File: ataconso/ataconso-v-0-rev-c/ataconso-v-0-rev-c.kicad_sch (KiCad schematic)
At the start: 22 parts, among them J1 Conn_02x05_Odd_Even, J2 AudioJack2_SwitchT, U1 TL072, U2 NE555D, U3 NE555D, U4 MC78L05_SO8

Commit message: agregar plantilla
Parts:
- removed U2, U3: NE555D, Package_DIP:DIP-8_W7.62mm_Socket_LongPads, symbol Timer:NE555D
- added U2: NA556, Package_SO:SOIC-14W_7.5x9mm_P1.27mm, symbol Timer:NA556
- C1, C2, C3, C4, C5, C6: footprint Capacitor_THT:C_Disc_D3.8mm_W2.6mm_P2.50mm -> (none)
- D1, D2: footprint Diode_THT:D_DO-41_SOD81_P10.16mm_Horizontal -> (none)
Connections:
- net +12V: now also U2.10 (~{RST}), U2.14 (VCC), U2.14 (VCC), U2.4 (~{RST})
- net GND: now also U2.7 (GND), U2.7 (GND)
- net at C5.1, R2.2: now also U2.12 (THRES), U2.13 (DISCH)
- net at C1.1, RV1.3: now also U2.2 (THRES), U2.6 (TRIG)
- net at C7.1: now also U2.9 (OUT)
- net at C6.1: now also U2.11 (CONT)
- net at R1.2, RV1.2: now also U2.1 (DISCH)
- net at C2.1: now also U2.3 (CONT)
- new net: U2.5 (OUT), U2.8 (TRIG)

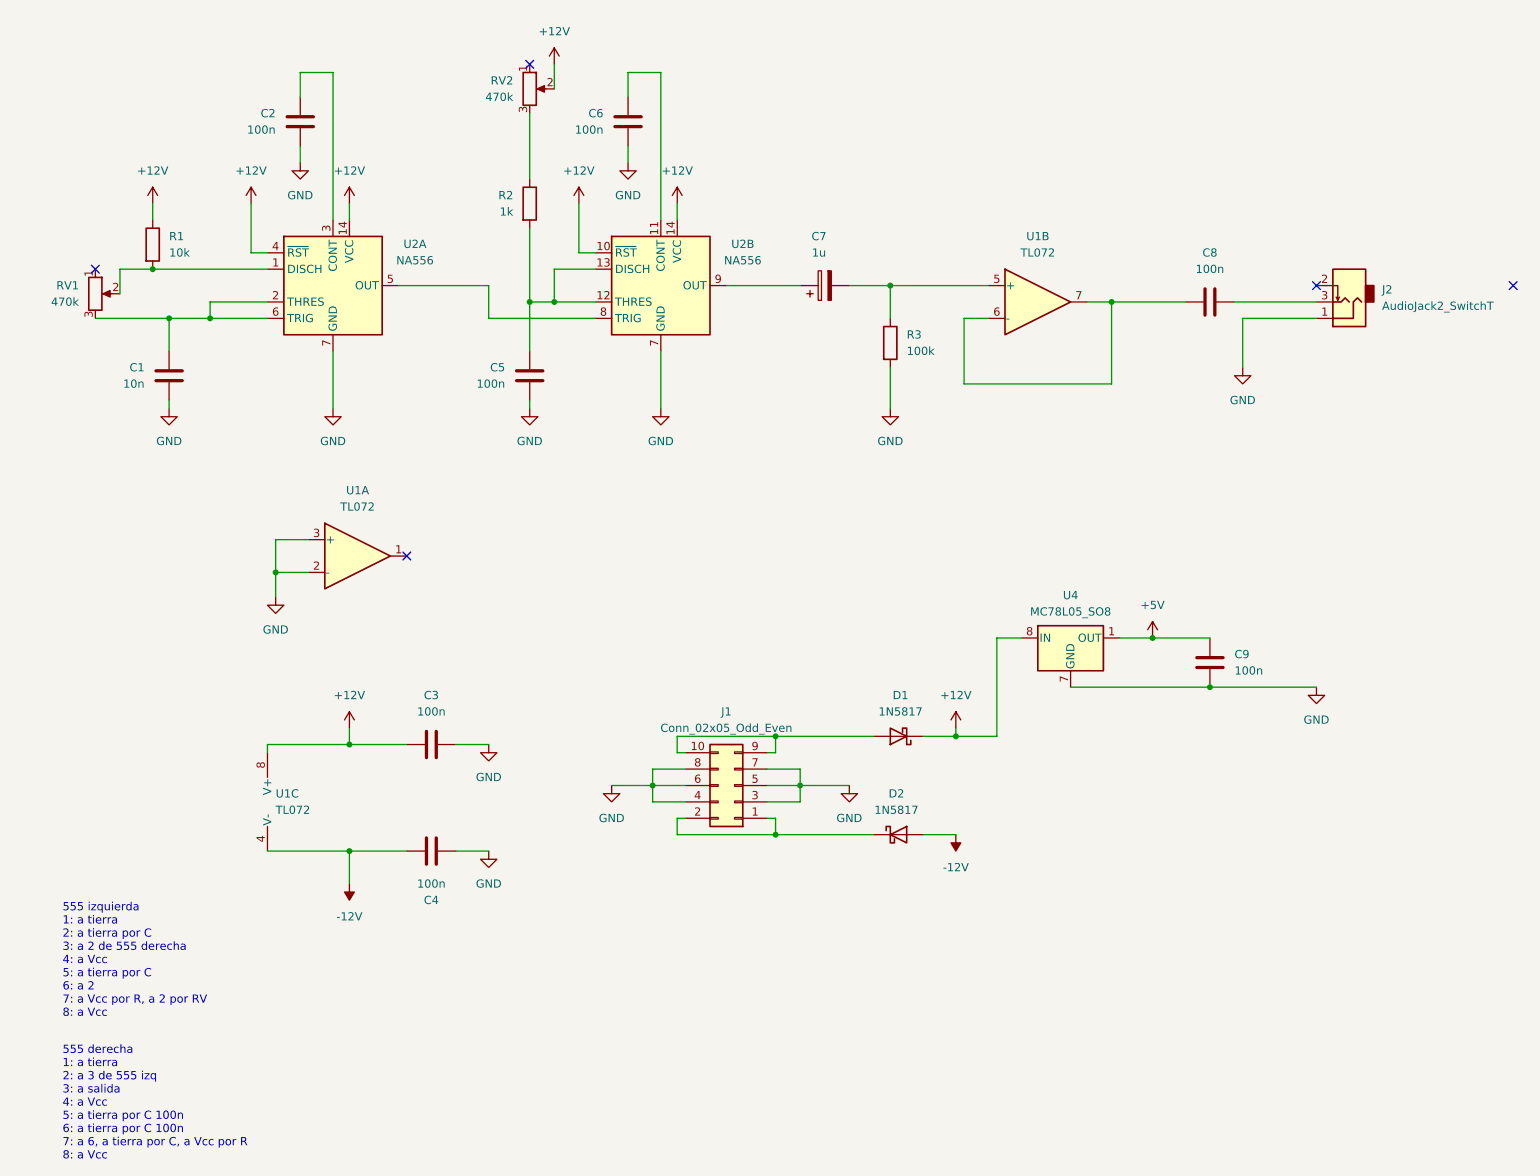
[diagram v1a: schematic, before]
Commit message: agregar plantillas
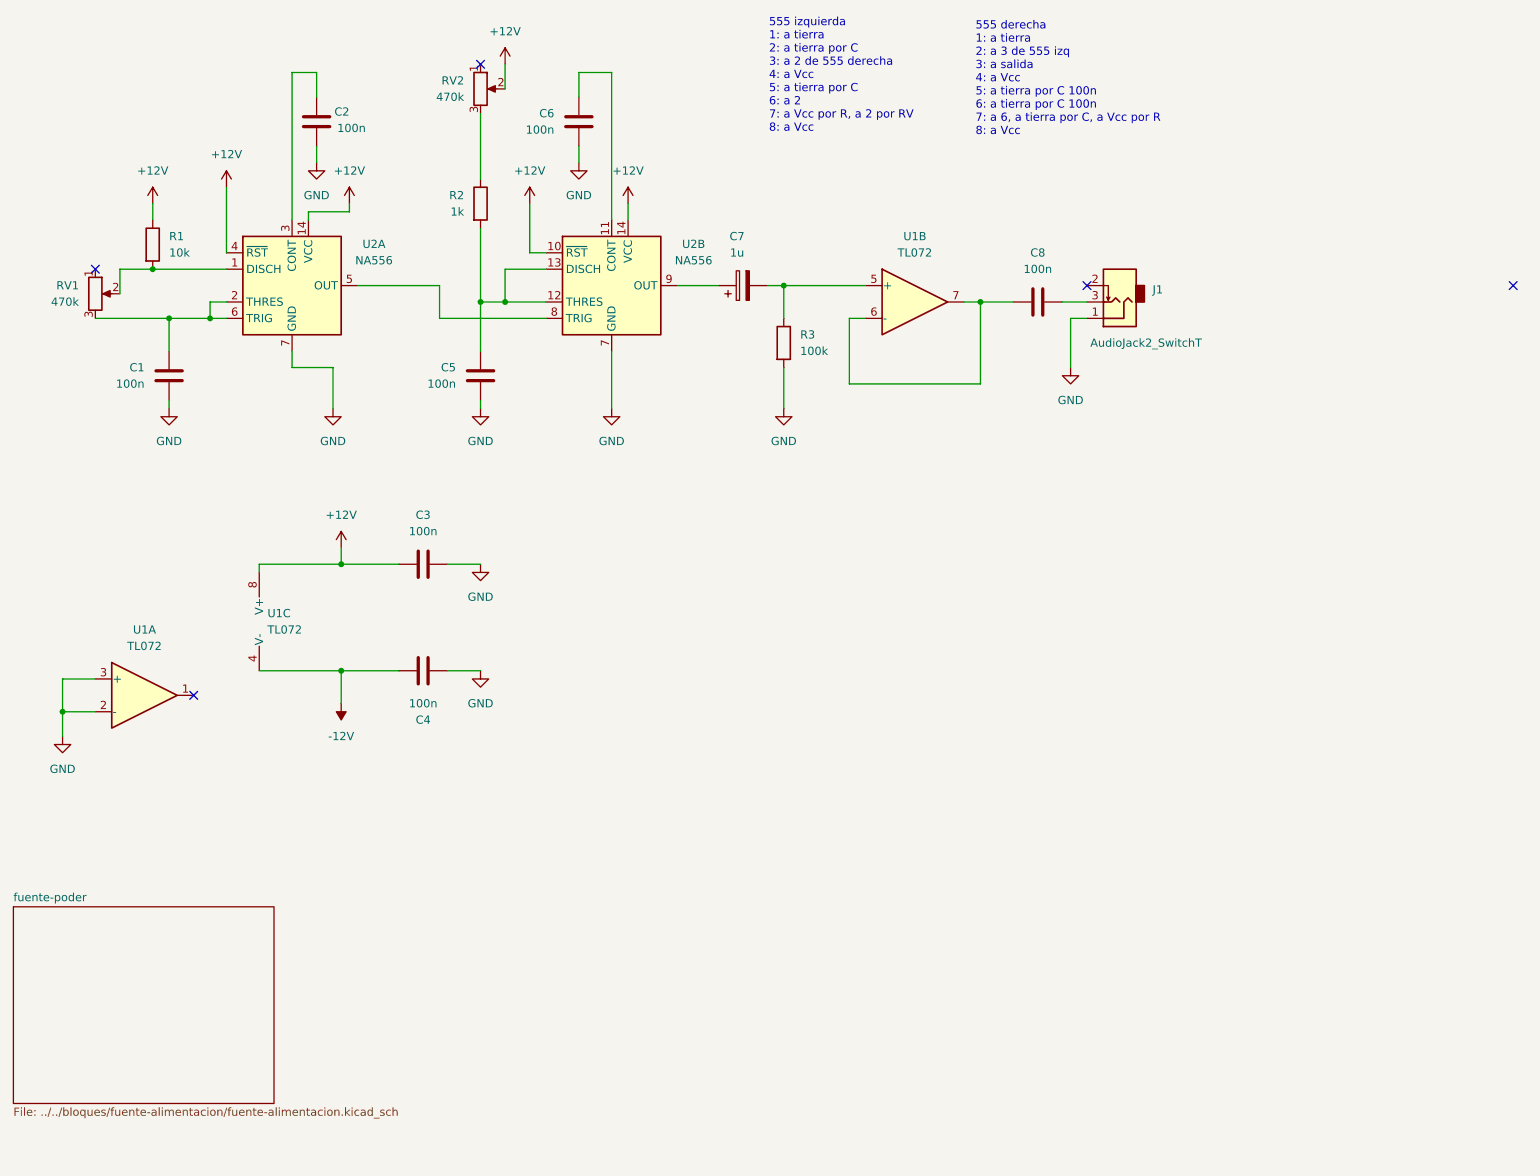
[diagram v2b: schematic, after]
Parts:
- removed C9: 100n, symbol Device:C
- removed D1, D2: 1N5817, symbol Diode:1N5817
- removed J1: Conn_02x05_Odd_Even, BYOM_General:IDC-Header_2x05_P2.54mm_Vertical, symbol Connector_Generic:Conn_02x05_Odd_Even
- removed U4: MC78L05_SO8, symbol Regulator_Linear:MC78L05_SO8
- C1: value 10n -> 100n
- renumbered J2 to J1
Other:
- added sheet fuente-poder (../../bloques/fuente-alimentacion/fuente-alimentacion.kicad_sch)
- title: (none) -> ataconso-v-0
- moved on the sheet: C2, C3, C4, C5, C6, C7, C8, J1, R2, R3, RV2, U1A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

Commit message: agregar parla relo ataconso con bibliotecas locales
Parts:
- J1: footprint BYOM_General:Jack_3.5mm_QingPu_WQP-PJ398SM_Vertical -> ataconso-v-0-rev-c:Jack_3.5mm_QingPu_WQP-PJ398SM_Vertical
- RV1, RV2: footprint BYOM_General:POT_TH_Alps_RK09K_Single_Vertical -> ataconso-v-0-rev-c:POT_TH_Alps_RK09K_Single_Vertical
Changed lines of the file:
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@@
 			)
 		)
-		(property "Footprint" "BYOM_General:Jack_3.5mm_QingPu_WQP-PJ398SM_Vertical"
+		(property "Footprint" "ataconso-v-0-rev-c:Jack_3.5mm_QingPu_WQP-PJ398SM_Vertical"
 			(at 180.34 60.96 0)
 			(hide yes)
@@
 			)
 		)
-		(property "Footprint" "BYOM_General:POT_TH_Alps_RK09K_Single_Vertical"
+		(property "Footprint" "ataconso-v-0-rev-c:POT_TH_Alps_RK09K_Single_Vertical"
 			(at 21.59 59.69 0)
 			(hide yes)
@@
 			)
 		)
-		(property "Footprint" "BYOM_General:POT_TH_Alps_RK09K_Single_Vertical"
+		(property "Footprint" "ataconso-v-0-rev-c:POT_TH_Alps_RK09K_Single_Vertical"
 			(at 81.28 27.94 0)
 			(hide yes)

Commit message: agregar blocks
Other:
- sheet fuente-poder: file ../../bloques/fuente-alimentacion/fuente-alimentacion.kicad_sch -> fuente-alimentacion.kicad_sch
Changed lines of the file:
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@@
 			)
 		)
-		(property "Sheetfile" "../../bloques/fuente-alimentacion/fuente-alimentacion.kicad_sch"
+		(property "Sheetfile" "fuente-alimentacion.kicad_sch"
 			(at 8.89 185.7506 0)
 			(show_name yes)

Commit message: avanzar en lcsc, huellas, stock
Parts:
- C1, C2, C3, C4, C5, C6, C8: footprint (none) -> Capacitor_SMD:C_0805_2012Metric_Pad1.18x1.45mm_HandSolder; LCSC (none) -> C49678
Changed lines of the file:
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@@
 			)
 		)
-		(property "Footprint" ""
+		(property "Footprint" "Capacitor_SMD:C_0805_2012Metric_Pad1.18x1.45mm_HandSolder"
 			(at 171.45 59.9948 0)
 			(hide yes)
@@
 		)
 		(property "Description" "Unpolarized capacitor"
+			(at 167.64 60.96 0)
+			(hide yes)
+			(show_name no)
+			(do_not_autoplace no)
+			(effects
+				(font
+					(size 1.27 1.27)
+				)
+			)
+		)
+		(property "LCSC" "C49678"
 			(at 167.64 60.96 0)
 			(hide yes)
@@
 			)
 		)
-		(property "Footprint" ""
+		(property "Footprint" "Capacitor_SMD:C_0805_2012Metric_Pad1.18x1.45mm_HandSolder"
 			(at 80.3148 76.2 0)
 			(hide yes)
@@
 		)
 		(property "Description" "Unpolarized capacitor"
+			(at 81.28 72.39 0)
+			(hide yes)
+			(show_name no)
+			(do_not_autoplace no)
+			(effects
+				(font
+					(size 1.27 1.27)
+				)
+			)
+		)
+		(property "LCSC" "C49678"
 			(at 81.28 72.39 0)
 			(hide yes)
@@
 			)
 		)
-		(property "Footprint" ""
+		(property "Footprint" "Capacitor_SMD:C_0805_2012Metric_Pad1.18x1.45mm_HandSolder"
 			(at 76.2 100.6348 0)
 			(hide yes)
@@
 		)
 		(property "Description" "Unpolarized capacitor"
+			(at 72.39 101.6 0)
+			(hide yes)
+			(show_name no)
+			(do_not_autoplace no)
+			(effects
+				(font
+					(size 1.27 1.27)
+				)
+			)
+		)
+		(property "LCSC" "C49678"
 			(at 72.39 101.6 0)
 			(hide yes)
@@
 			)
 		)
-		(property "Footprint" ""
+		(property "Footprint" "Capacitor_SMD:C_0805_2012Metric_Pad1.18x1.45mm_HandSolder"
 			(at 32.0548 76.2 0)
 			(hide yes)
@@
 		)
 		(property "Description" "Unpolarized capacitor"
+			(at 33.02 72.39 0)
+			(hide yes)
+			(show_name no)
+			(do_not_autoplace no)
+			(effects
+				(font
+					(size 1.27 1.27)
+				)
+			)
+		)
+		(property "LCSC" "C49678"
 			(at 33.02 72.39 0)
 			(hide yes)
@@
 			)
 		)
-		(property "Footprint" ""
+		(property "Footprint" "Capacitor_SMD:C_0805_2012Metric_Pad1.18x1.45mm_HandSolder"
 			(at 54.9148 36.83 0)
 			(hide yes)
@@
 		)
 		(property "Description" "Unpolarized capacitor"
+			(at 55.88 33.02 0)
+			(hide yes)
+			(show_name no)
+			(do_not_autoplace no)
+			(effects
+				(font
+					(size 1.27 1.27)
+				)
+			)
+		)
+		(property "LCSC" "C49678"
 			(at 55.88 33.02 0)
 			(hide yes)
@@
 			)
 		)
-		(property "Footprint" ""
+		(property "Footprint" "Capacitor_SMD:C_0805_2012Metric_Pad1.18x1.45mm_HandSolder"
 			(at 95.5548 36.83 0)
 			(hide yes)
@@
 		)
 		(property "Description" "Unpolarized capacitor"
+			(at 96.52 33.02 0)
+			(hide yes)
+			(show_name no)
+			(do_not_autoplace no)
+			(effects
+				(font
+					(size 1.27 1.27)
+				)
+			)
+		)
+		(property "LCSC" "C49678"
 			(at 96.52 33.02 0)
 			(hide yes)
@@
 			)
 		)
-		(property "Footprint" ""
+		(property "Footprint" "Capacitor_SMD:C_0805_2012Metric_Pad1.18x1.45mm_HandSolder"
 			(at 76.2 119.0752 0)
 			(hide yes)
@@
 			(at 72.39 118.11 0)
 			(hide yes)
+			(show_name no)
+			(do_not_autoplace no)
+			(effects
+				(font
+					(size 1.27 1.27)
+				)
+			)
+		)
+		(property "LCSC" "C49678"
+			(at 72.39 118.11 0)
+			(hide yes)
